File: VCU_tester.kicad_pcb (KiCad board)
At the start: 2 copper layers, 200 x 159 mm, 125 parts, among them J1 Conn_01x04_Male, J10 DB9_Male, J11 DB9_Male, J12 Conn_01x08_Male, J13 Conn_01x08_Male, J14 USB_C_Receptacle, J15 USB_B_Micro, J16 Conn_01x05_Male, J2 Screw_Terminal_01x02, J3 DB9_Male, J4 DB9_Male, J5 DB9_Male, J500 Conn_01x10_Female, J501 Conn_01x08_Female, J502 Conn_01x08_Female, J503 Conn_01x08_Female, J504 Conn_01x08_Female, J505 Conn_01x08_Female, J507 Conn_02x18_Odd_Even, J6 DB9_Male, J7 Conn_01x04_Male, J8 DB9_Male, J9 DB9_Male, P8 BeagleBone_Black_Header, P9 BeagleBone_Black_Header, U1 REF3020, U2 MAX3232, U3 TCAN1042HVD, U4 MAX3232, U5 TCAN1042HVD, U6 DS3231MZ, U7 DS3231MZ

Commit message: gerbers and pdfs
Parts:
- moved G*** 133.8 mm to (154.1, 60.5)
- moved C18 132.7 mm to (164.6, 103.9)
- moved J12 132.7 mm to (262.1, 115.0)
- moved J16 132.7 mm to (230.3, 125.1)
- moved J501 132.7 mm to (250.1, 196.6)
- moved J502 132.7 mm to (250.1, 173.7)
- moved J504 132.7 mm to (250.1, 150.9)
- moved J7 132.7 mm to (283.6, 115.0)
- moved R9 132.7 mm to (184.9, 172.8)
- moved REF** 132.7 mm to (250.1, 196.6)
- moved TP1 132.7 mm to (283.6, 107.5)
- moved TP32 132.7 mm to (270.6, 101.9)
- moved TP34 132.7 mm to (275.6, 101.9)
- moved TP36 132.7 mm to (270.6, 94.4)
- moved TP38 132.7 mm to (275.6, 94.4)
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
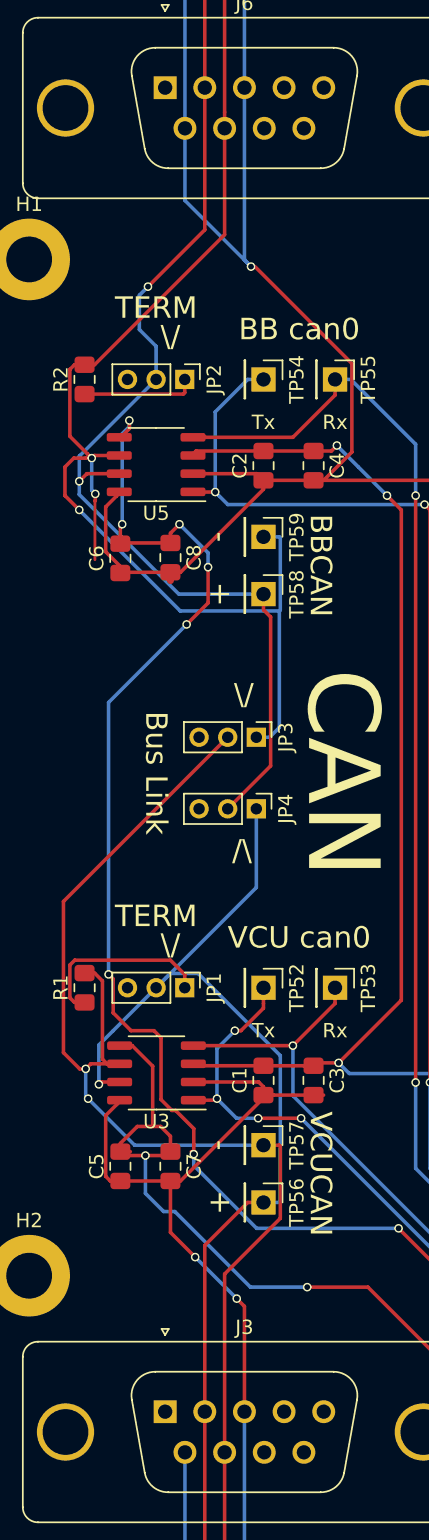
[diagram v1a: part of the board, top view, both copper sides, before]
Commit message: CAN pin fix, need to ground pour and done
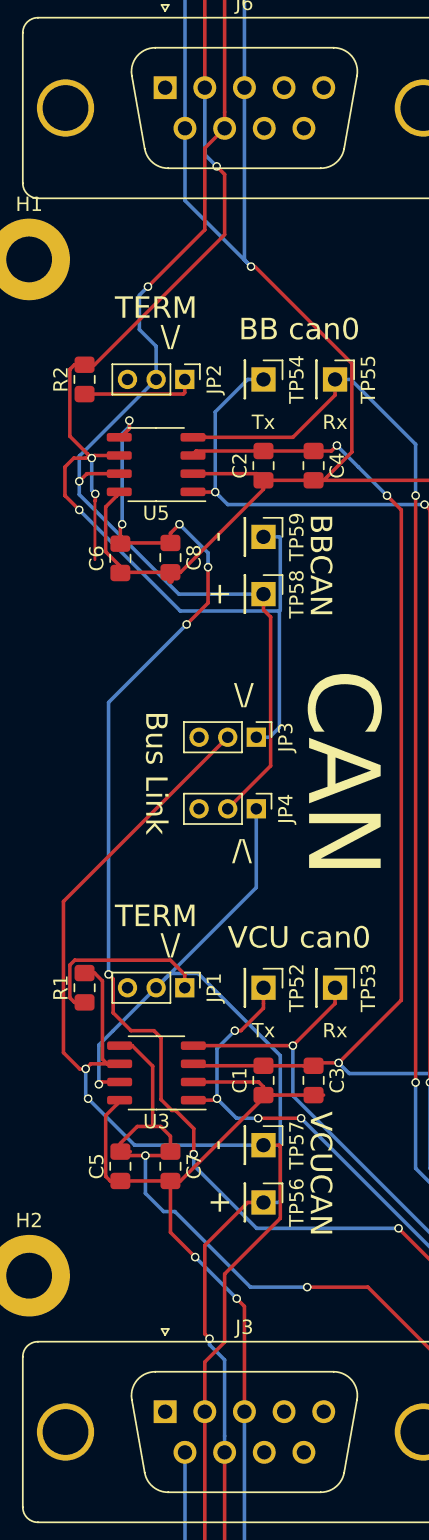
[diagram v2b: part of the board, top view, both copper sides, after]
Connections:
- J3 pad 2: VCUCAN+ -> VCUCAN-
- J3 pad 7: VCUCAN- -> VCUCAN+
- J4 pad 2: VCUCAN+ -> VCUCAN-
- J4 pad 7: VCUCAN- -> VCUCAN+
- J5 pad 2: BBCAN+ -> BBCAN-
- J5 pad 7: BBCAN- -> BBCAN+
- J6 pad 2: BBCAN+ -> BBCAN-
- J6 pad 7: BBCAN- -> BBCAN+
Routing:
- net BBCAN-: track 97.1 -> 100.5 mm, vias 3 -> 4
- net VCUCAN+: track 85.2 -> 88.7 mm, vias 1 -> 2
- net BBCAN+: track 88.3 -> 86.1 mm
- net VCUCAN-: track 99.8 -> 97.6 mm
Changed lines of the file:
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@@
     (thickness 1.6)
     (drawings 126)
-    (tracks 2163)
+    (tracks 2176)
     (zones 0)
     (modules 125)
@@
     (31 B.Cu signal)
     (32 B.Adhes user)
-    (33 F.Adhes user hide)
+    (33 F.Adhes user)
     (34 B.Paste user)
     (35 F.Paste user)
@@
     (pad_drill 0)
     (pad_to_mask_clearance 0)
-    (aux_axis_origin 78 111.2)
+    (aux_axis_origin 108 205)
     (grid_origin 78 111)
     (visible_elements 7FFFFFFF)
@@
       (net 92 "Net-(J6-Pad1)"))
     (pad 2 thru_hole circle (at 2.77 0) (size 1.6 1.6) (drill 1) (layers *.Cu *.Mask)
-      (net 44 BBCAN+))
+      (net 45 BBCAN-))
     (pad 3 thru_hole circle (at 5.54 0) (size 1.6 1.6) (drill 1) (layers *.Cu *.Mask)
       (net 1 GNDD))
@@
       (net 1 GNDD))
     (pad 7 thru_hole circle (at 4.155 2.84) (size 1.6 1.6) (drill 1) (layers *.Cu *.Mask)
-      (net 45 BBCAN-))
+      (net 44 BBCAN+))
     (pad 8 thru_hole circle (at 6.925 2.84) (size 1.6 1.6) (drill 1) (layers *.Cu *.Mask)
       (net 241 "Net-(J6-Pad8)"))
@@
       (net 89 "Net-(J5-Pad1)"))
     (pad 2 thru_hole circle (at 2.77 0) (size 1.6 1.6) (drill 1) (layers *.Cu *.Mask)
-      (net 44 BBCAN+))
+      (net 45 BBCAN-))
     (pad 3 thru_hole circle (at 5.54 0) (size 1.6 1.6) (drill 1) (layers *.Cu *.Mask)
       (net 1 GNDD))
@@
       (net 1 GNDD))
     (pad 7 thru_hole circle (at 4.155 2.84) (size 1.6 1.6) (drill 1) (layers *.Cu *.Mask)
-      (net 45 BBCAN-))
+      (net 44 BBCAN+))
     (pad 8 thru_hole circle (at 6.925 2.84) (size 1.6 1.6) (drill 1) (layers *.Cu *.Mask)
       (net 239 "Net-(J5-Pad8)"))
@@
       (net 83 "Net-(J3-Pad1)"))
     (pad 2 thru_hole circle (at 2.77 0) (size 1.6 1.6) (drill 1) (layers *.Cu *.Mask)
-      (net 42 VCUCAN+))
+      (net 43 VCUCAN-))
     (pad 3 thru_hole circle (at 5.54 0) (size 1.6 1.6) (drill 1) (layers *.Cu *.Mask)
       (net 1 GNDD))
@@
       (net 1 GNDD))
     (pad 7 thru_hole circle (at 4.155 2.84) (size 1.6 1.6) (drill 1) (layers *.Cu *.Mask)
-      (net 43 VCUCAN-))
+      (net 42 VCUCAN+))
     (pad 8 thru_hole circle (at 6.925 2.84) (size 1.6 1.6) (drill 1) (layers *.Cu *.Mask)
       (net 243 "Net-(J3-Pad8)"))
@@
       (net 86 "Net-(J4-Pad1)"))
     (pad 2 thru_hole circle (at 2.77 0) (size 1.6 1.6) (drill 1) (layers *.Cu *.Mask)
-      (net 42 VCUCAN+))
+      (net 43 VCUCAN-))
     (pad 3 thru_hole circle (at 5.54 0) (size 1.6 1.6) (drill 1) (layers *.Cu *.Mask)
       (net 1 GNDD))
@@
       (net 1 GNDD))
     (pad 7 thru_hole circle (at 4.155 2.84) (size 1.6 1.6) (drill 1) (layers *.Cu *.Mask)
-      (net 43 VCUCAN-))
+      (net 42 VCUCAN+))
     (pad 8 thru_hole circle (at 6.925 2.84) (size 1.6 1.6) (drill 1) (layers *.Cu *.Mask)
       (net 245 "Net-(J4-Pad8)"))
@@
   (segment (start 126.5701 138.3824) (end 119.5701 145.3824) (width 0.25) (layer B.Cu) (net 42))
   (segment (start 126.5701 132.8824) (end 126.5701 138.3824) (width 0.25) (layer B.Cu) (net 42))
-  (segment (start 122.97 175) (end 122.97 195) (width 0.25) (layer F.Cu) (net 42))
+  (segment (start 122.97 175) (end 122.97 195) (width 0.25) (layer F.Cu) (net 43))
   (segment (start 125.9701 160.3824) (end 127.0701 160.3824) (width 0.25) (layer F.Cu) (net 42))
   (segment (start 122.97 163.3825) (end 125.9701 160.3824) (width 0.25) (layer F.Cu) (net 42))
-  (segment (start 122.97 175) (end 122.97 163.3825) (width 0.25) (layer F.Cu) (net 42))
   (via (at 114.8201 153.1324) (size 0.6) (drill 0.4) (layers F.Cu B.Cu) (net 43))
   (segment (start 115.8201 150.3724) (end 116.1451 150.6974) (width 0.25) (layer F.Cu) (net 43))
@@
   (segment (start 114.225737 151.049999) (end 113.095081 149.919343) (width 0.25) (layer F.Cu) (net 43))
   (segment (start 114.650001 151.049999) (end 114.225737 151.049999) (width 0.25) (layer F.Cu) (net 43))
-  (segment (start 124.355 197.84) (end 124.355 177.84) (width 0.25) (layer F.Cu) (net 43))
+  (segment (start 124.355 197.84) (end 124.355 177.84) (width 0.25) (layer F.Cu) (net 42))
+  (via (at 123.3 169.9) (size 0.6) (drill 0.4) (layers F.Cu B.Cu) (net 42))
+  (segment (start 122.97 163.3825) (end 122.97 169.57) (width 0.25) (layer F.Cu) (net 42))
+  (segment (start 122.97 169.57) (end 123.3 169.9) (width 0.25) (layer F.Cu) (net 42))
+  (segment (start 124.355 176.70863) (end 124.355 177.84) (width 0.25) (layer B.Cu) (net 42))
+  (segment (start 124.355 171.379264) (end 124.355 176.70863) (width 0.25) (layer B.Cu) (net 42))
+  (segment (start 123.3 170.324264) (end 124.355 171.379264) (width 0.25) (layer B.Cu) (net 42))
+  (segment (start 123.3 169.9) (end 123.3 170.324264) (width 0.25) (layer B.Cu) (net 42))
   (segment (start 128.245101 156.457401) (end 128.1701 156.3824) (width 0.25) (layer F.Cu) (net 43))
   (segment (start 128.245101 161.492401) (end 128.245101 156.457401) (width 0.25) (layer F.Cu) (net 43))
   (segment (start 128.1701 156.3824) (end 127.0701 156.3824) (width 0.25) (layer F.Cu) (net 43))
   (segment (start 124.355 165.382502) (end 128.245101 161.492401) (width 0.25) (layer F.Cu) (net 43))
-  (segment (start 124.355 177.84) (end 124.355 165.382502) (width 0.25) (layer F.Cu) (net 43))
+  (segment (start 124.355 165.382502) (end 124.355 170.145) (width 0.25) (layer F.Cu) (net 43))
+  (segment (start 122.97 171.53) (end 122.97 175) (width 0.25) (layer F.Cu) (net 43))
+  (segment (start 124.355 170.145) (end 122.97 171.53) (width 0.25) (layer F.Cu) (net 43))
   (segment (start 119.5701 102.8824) (end 114.270101 108.182399) (width 0.25) (layer B.Cu) (net 44))
   (segment (start 127.0701 118.9824) (end 127.0701 117.8824) (width 0.25) (layer F.Cu) (net 44))
@@
   (segment (start 114.2 108.2525) (end 114.270101 108.182399) (width 0.25) (layer B.Cu) (net 44))
   (segment (start 114.2 110) (end 114.2 108.2525) (width 0.25) (layer B.Cu) (net 44))
-  (segment (start 122.97 63.63137) (end 122.97 82.5) (width 0.25) (layer F.Cu) (net 44))
-  (segment (start 122.97 62.5) (end 122.97 63.63137) (width 0.25) (layer F.Cu) (net 44))
+  (segment (start 122.97 63.63137) (end 122.97 82.5) (width 0.25) (layer F.Cu) (net 45))
+  (segment (start 122.97 62.5) (end 122.97 63.63137) (width 0.25) (layer F.Cu) (net 45))
   (via (at 119 96.4) (size 0.6) (drill 0.4) (layers F.Cu B.Cu) (net 44))
-  (segment (start 122.97 82.5) (end 122.97 92.43) (width 0.25) (layer F.Cu) (net 44))
   (segment (start 122.97 92.43) (end 119 96.4) (width 0.25) (layer F.Cu) (net 44))
   (segment (start 119 96.4) (end 118.4 97) (width 0.25) (layer B.Cu) (net 44))
@@
   (segment (start 113.2 109) (end 113.2 111) (width 0.25) (layer F.Cu) (net 45))
   (segment (start 113.2 111) (end 114.2 112) (width 0.25) (layer F.Cu) (net 45))
-  (segment (start 124.355 84.20863) (end 124.355 65.34) (width 0.25) (layer F.Cu) (net 45))
-  (segment (start 124.355 85.34) (end 124.355 84.20863) (width 0.25) (layer F.Cu) (net 45))
+  (segment (start 124.355 84.20863) (end 124.355 65.34) (width 0.25) (layer F.Cu) (net 44))
+  (segment (start 124.355 85.34) (end 124.355 84.20863) (width 0.25) (layer F.Cu) (net 44))
+  (segment (start 122.97 86.725) (end 124.355 85.34) (width 0.25) (layer F.Cu) (net 44))
+  (segment (start 122.97 92.43) (end 122.97 86.725) (width 0.25) (layer F.Cu) (net 44))
   (segment (start 115.2701 101.8574) (end 114.5701 101.8574) (width 0.25) (layer F.Cu) (net 45))
   (segment (start 124.355 92.7725) (end 115.2701 101.8574) (width 0.25) (layer F.Cu) (net 45))
-  (segment (start 124.355 85.34) (end 124.355 92.7725) (width 0.25) (layer F.Cu) (net 45))
+  (segment (start 124.355 92.7725) (end 124.355 88.555) (width 0.25) (layer F.Cu) (net 45))
+  (via (at 123.8 88) (size 0.6) (drill 0.4) (layers F.Cu B.Cu) (net 45))
+  (segment (start 124.355 88.555) (end 123.8 88) (width 0.25) (layer F.Cu) (net 45))
+  (segment (start 122.97 87.17) (end 122.97 82.5) (width 0.25) (layer B.Cu) (net 45))
+  (segment (start 123.8 88) (end 122.97 87.17) (width 0.25) (layer B.Cu) (net 45))
   (segment (start 117.7701 156.8324) (end 117.0701 156.8324) (width 0.25) (layer F.Cu) (net 46))
   (segment (start 245.6251 103.8274) (end 245.5701 103.8824) (width 0.25) (layer F.Cu) (net 46))

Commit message: ground plane, checked, ready to go?
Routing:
- net GNDD: track 1094.2 -> 1152.1 mm, vias 21 -> 137
- net +5V: track 447.9 -> 446.6 mm
- added copper zone on B.Cu, net GNDD
- added copper zone on F.Cu, net GNDD

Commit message: silkscreen + neater copper fills, ready to go?
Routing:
- net GNDD: vias 137 -> 182
- net (no net): vias 0 -> 1
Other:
- board text added: "."
- board text added: "BB->VCU UART1-UART3"
- board text removed: "BB->VCU UART1"
